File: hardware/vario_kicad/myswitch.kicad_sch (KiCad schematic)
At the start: 3 parts

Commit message: minor updates
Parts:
- added S3: ~, symbol_lib:TS-1187A-B-A-B_switch, symbol New_Library:switch
- renumbered C15 to C16, R30 to R31, R32 to R33
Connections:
- net SWITCH_OUT: now also S3.3 (C)
- net at R33.2: now also S3.1 (A)
- no-connect marks 0 -> 2
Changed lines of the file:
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@@
 		(color 0 0 0 0)
 	)
+	(no_connect
+		(at 80.01 80.01)
+	)
+	(no_connect
+		(at 80.01 82.55)
+	)
 	(wire
 		(pts
@@
 	(wire
 		(pts
-			(xy 67.31 86.36) (xy 67.31 88.9)
+			(xy 67.31 82.55) (xy 67.31 88.9)
 		)
 		(stroke
@@
 	(wire
 		(pts
+			(xy 67.31 73.66) (xy 67.31 80.01)
+		)
+		(stroke
+			(width 0)
+			(type default)
+		)
+	)
+	(wire
+		(pts
 			(xy 54.61 101.6) (xy 67.31 101.6)
 		)
@@
 		(pts
 			(xy 67.31 88.9) (xy 54.61 88.9)
-		)
-		(stroke
-			(width 0)
-			(type default)
-		)
-	)
-	(wire
-		(pts
-			(xy 67.31 73.66) (xy 67.31 76.2)
 		)
 		(stroke
@@
 			)
 			(justify left)
+		)
+	)
+	(symbol
+		(lib_id "New_Library:switch")
+		(at 73.66 81.28 0)
+		(unit 1)
+		(exclude_from_sim no)
+		(in_bom yes)
+		(on_board yes)
+		(dnp no)
+		(fields_autoplaced yes)
+		(property "Reference" "S3"
+			(at 73.66 74.93 0)
+			(effects
+				(font
+					(size 1.27 1.27)
+				)
+			)
+		)
+		(property "Value" "~"
+			(at 73.66 77.47 0)
+			(effects
+				(font
+					(size 1.27 1.27)
+				)
+			)
+		)
+		(property "Footprint" "symbol_lib:TS-1187A-B-A-B_switch"
+			(at 73.66 87.122 0)
+			(effects
+				(font
+					(size 1.27 1.27)
+				)
+				(hide yes)
+			)
+		)
+		(property "Datasheet" ""
+			(at 73.66 81.28 0)
+			(effects
+				(font
+					(size 1.27 1.27)
+				)
+				(hide yes)
+			)
+		)
+		(property "Description" ""
+			(at 73.66 81.28 0)
+			(effects
+				(font
+					(size 1.27 1.27)
+				)
+				(hide yes)
+			)
+		)
+		(pin "3"
+		)
+		(pin "4"
+		)
+		(pin "2"
+		)
+		(pin "1"
+		)
+		(instances
+			(project ""
+				(path "/50389aff-b244-451e-8e3a-c5addd2215e1/1d6f8f38-55c9-4e4a-ab41-42426d9c3f80"
+					(reference "S2")
+					(unit 1)
+				)
+				(path "/50389aff-b244-451e-8e3a-c5addd2215e1/976879c2-7f90-4e8e-bed0-613d5ac3800c"
+					(reference "S3")
+					(unit 1)
+				)
+				(path "/50389aff-b244-451e-8e3a-c5addd2215e1/ae77d581-7721-4c08-a977-60b9367d2173"
+					(reference "S1")
+					(unit 1)
+				)
+			)
 		)
 	)
@@
 		(dnp no)
 		(fields_autoplaced yes)
-		(property "Reference" "R32"
+		(property "Reference" "R33"
 			(at 69.85 68.5799 0)
 			(effects
@@
 		(dnp no)
 		(fields_autoplaced yes)
-		(property "Reference" "#PWR38"
+		(property "Reference" "#PWR39"
 			(at 67.31 110.49 0)
 			(effects
@@
 		(dnp no)
 		(fields_autoplaced yes)
-		(property "Reference" "R30"
+		(property "Reference" "R31"
 			(at 57.15 93.9799 0)
 			(effects
@@
 		(dnp no)
 		(fields_autoplaced yes)
-		(property "Reference" "#PWR36"
+		(property "Reference" "#PWR37"
 			(at 67.31 67.31 0)
 			(effects
@@
 		(dnp no)
 		(fields_autoplaced yes)
-		(property "Reference" "C15"
+		(property "Reference" "C16"
 			(at 71.12 93.9799 0)
 			(effects

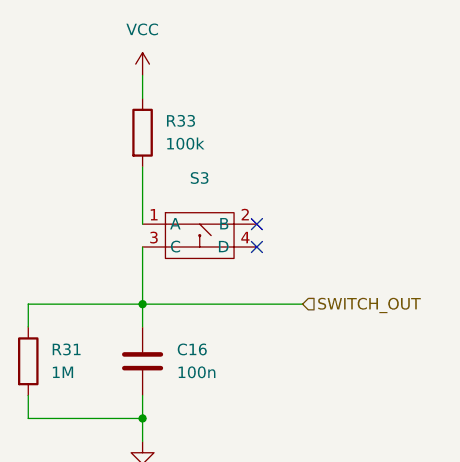
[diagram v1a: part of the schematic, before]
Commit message: update some component footprints
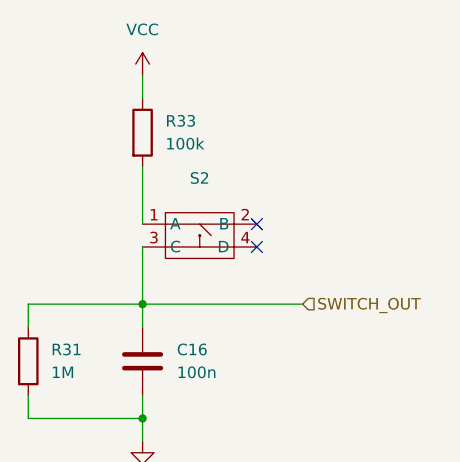
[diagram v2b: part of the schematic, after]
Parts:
- C16: footprint (none) -> Capacitor_SMD:C_0603_1608Metric
- renumbered S3 to S2
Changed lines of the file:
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@@
 		(dnp no)
 		(fields_autoplaced yes)
-		(property "Reference" "S3"
+		(property "Reference" "S2"
 			(at 73.66 74.93 0)
 			(effects
@@
 			)
 		)
-		(property "Datasheet" ""
+		(property "Datasheet" "https://www.lcsc.com/product-detail/Tactile-Switches_XKB-Connection-TS-1187A-B-A-B_C318884.html?s_z=n_ts-11-87a"
 			(at 73.66 81.28 0)
 			(effects
@@
 			)
 		)
-		(property "Footprint" ""
+		(property "Footprint" "Capacitor_SMD:C_0603_1608Metric"
 			(at 68.2752 99.06 0)
 			(effects

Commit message: update footprints, add LSE oscillator
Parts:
- R31, R33: footprint (none) -> Resistor_SMD:R_0402_1005Metric
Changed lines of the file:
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@@
 			)
 		)
-		(property "Footprint" ""
+		(property "Footprint" "Resistor_SMD:R_0402_1005Metric"
 			(at 65.532 69.85 90)
 			(effects
@@
 			)
 		)
-		(property "Footprint" ""
+		(property "Footprint" "Resistor_SMD:R_0402_1005Metric"
 			(at 52.832 95.25 90)
 			(effects

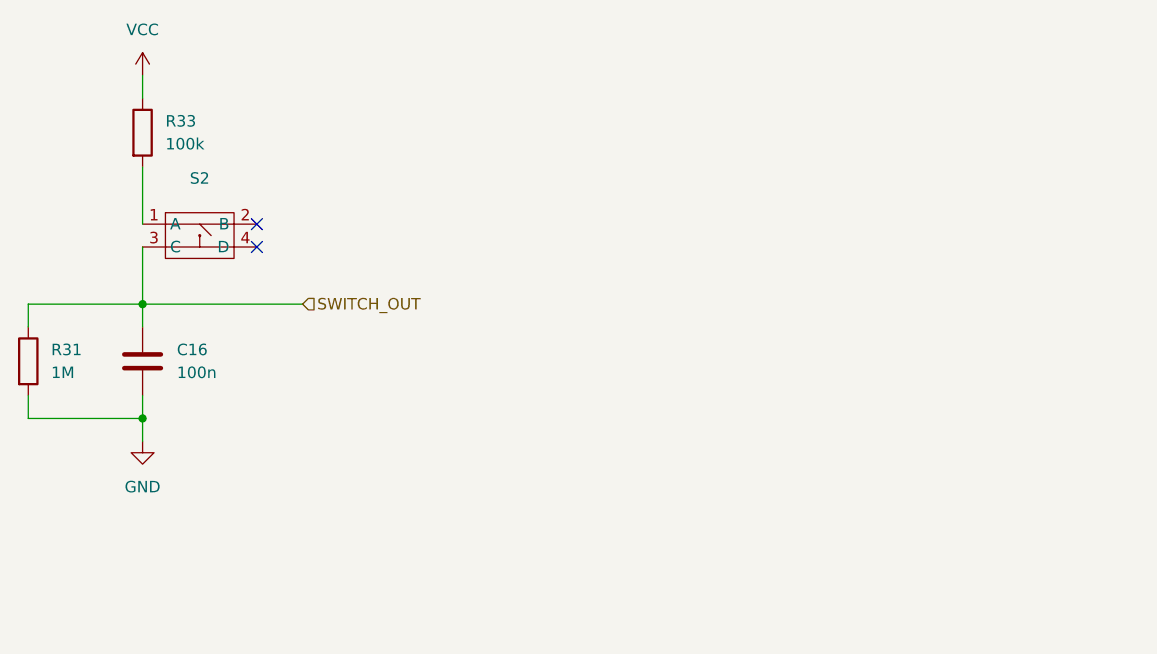
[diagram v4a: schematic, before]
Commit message: better switch debounce
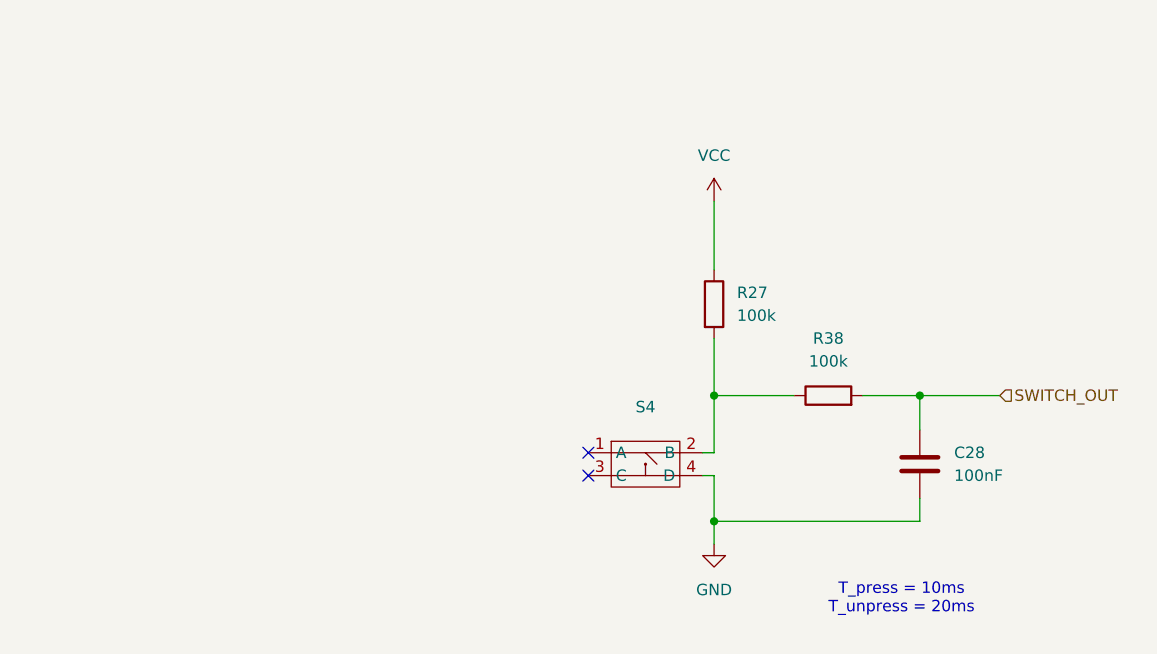
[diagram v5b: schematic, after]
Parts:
- removed C16: 100n, Capacitor_SMD:C_0603_1608Metric, symbol Device:C
- removed R31: 1M, Resistor_SMD:R_0402_1005Metric, symbol Device:R
- removed R33: 100k, Resistor_SMD:R_0402_1005Metric, symbol Device:R
- removed S2: ~, symbol_lib:TS-1187A-B-A-B_switch, symbol New_Library:switch
- added C28: 100nF, Capacitor_SMD:C_0603_1608Metric, symbol Device:C
- added R27, R38: 100k, Resistor_SMD:R_0402_1005Metric, symbol Device:R
- added S4: ~, symbol_lib:TS-1187A-B-A-B_switch, symbol New_Library:switch
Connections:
- net GND: now also C28.2, S4.4 (D)
- net SWITCH_OUT: now also C28.1, R38.2
- net VCC: now also R27.1
- new net: R27.2, R38.1, S4.2 (B)
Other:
- note added: "T_press = 10ms T_unpress = 20ms"

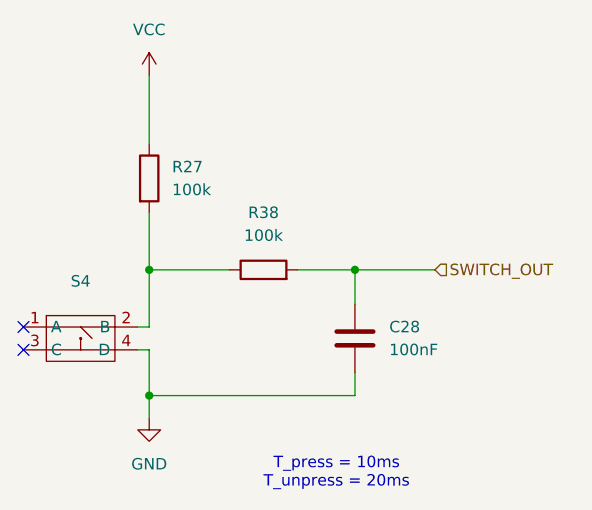
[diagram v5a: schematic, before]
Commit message: update switch de-bouncing
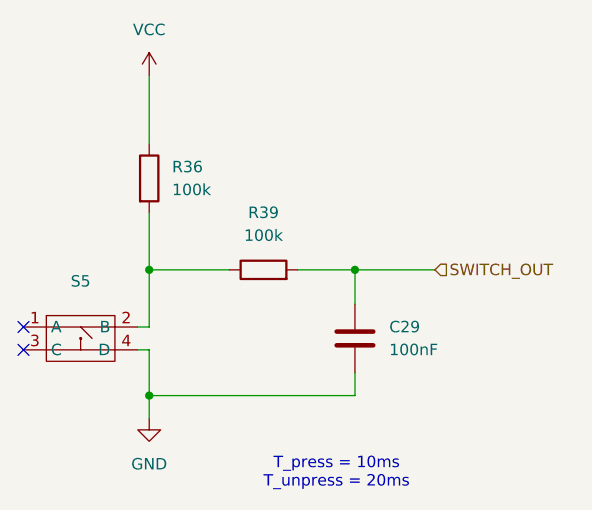
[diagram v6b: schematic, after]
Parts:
- renumbered C28 to C29, R27 to R36, R38 to R39, S4 to S5
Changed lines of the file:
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@@
 		(dnp no)
 		(fields_autoplaced yes)
-		(property "Reference" "R38"
+		(property "Reference" "R39"
 			(at 143.51 92.71 90)
 			(effects
@@
 		(dnp no)
 		(fields_autoplaced yes)
-		(property "Reference" "R27"
+		(property "Reference" "R36"
 			(at 133.35 87.6299 0)
 			(effects
@@
 		(dnp no)
 		(fields_autoplaced yes)
-		(property "Reference" "S4"
+		(property "Reference" "S5"
 			(at 123.19 100.33 0)
 			(effects
@@
 		(dnp no)
 		(fields_autoplaced yes)
-		(property "Reference" "#PWR17"
+		(property "Reference" "#PWR24"
 			(at 130.81 121.92 0)
 			(effects
@@
 		(dnp no)
 		(fields_autoplaced yes)
-		(property "Reference" "#PWR49"
+		(property "Reference" "#PWR50"
 			(at 130.81 81.28 0)
 			(effects
@@
 		(dnp no)
 		(fields_autoplaced yes)
-		(property "Reference" "C28"
+		(property "Reference" "C29"
 			(at 157.48 105.4099 0)
 			(effects

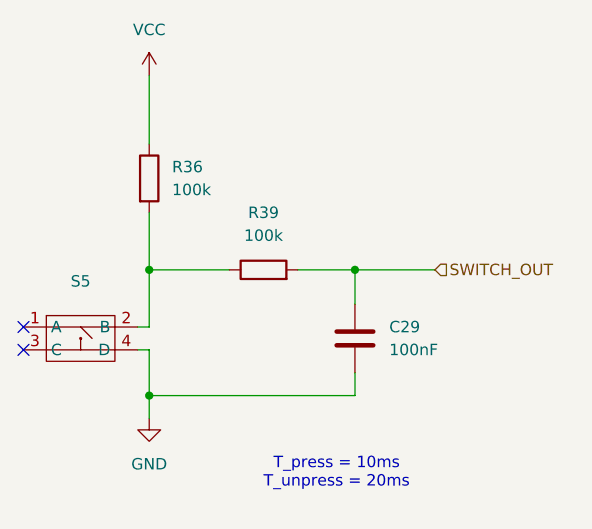
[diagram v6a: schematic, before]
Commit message: fix memory schematic, update button switches
- fix miso/mosi mistake: miso->miso, mosi->mosi
- WKUP1 needs a rising edge to wake up the MCU, so all switch logic was
  reversed
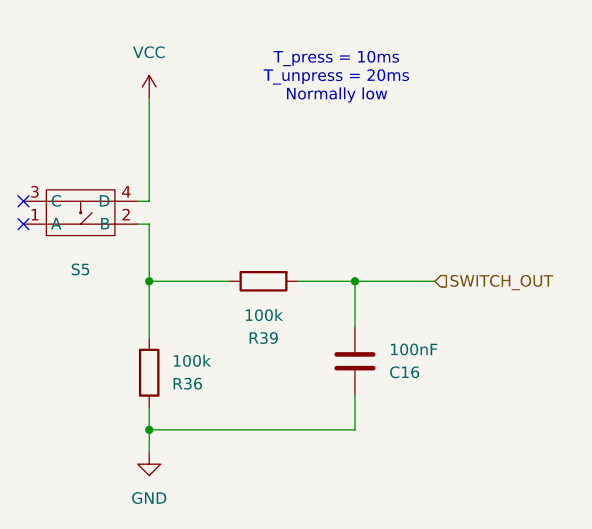
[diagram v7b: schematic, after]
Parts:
- removed C29: 100nF, Capacitor_SMD:C_0603_1608Metric, symbol Device:C
- added C16: 100nF, Capacitor_SMD:C_0603_1608Metric, symbol Device:C
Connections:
- net GND: now also R36.1, C16.1; no longer S5.4 (D)
- net SWITCH_OUT: now also C16.2
- net VCC: now also S5.4 (D); no longer R36.1
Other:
- note added: "T_press = 10ms T_unpress = 20ms Normally low"
- note removed: "T_press = 10ms T_unpress = 20ms"
- moved on the sheet: R36, R39, S5

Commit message: minor changes
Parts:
- renumbered C16 to C17
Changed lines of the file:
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@@
 		(dnp no)
 		(fields_autoplaced yes)
-		(property "Reference" "#PWR17"
+		(property "Reference" "#PWR24"
 			(at 130.81 83.82 0)
 			(effects
@@
 		(dnp no)
 		(fields_autoplaced yes)
-		(property "Reference" "C16"
+		(property "Reference" "C17"
 			(at 157.48 110.4901 0)
 			(effects
